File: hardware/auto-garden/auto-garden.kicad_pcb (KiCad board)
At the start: 2 copper layers, 71.1 x 55.9 mm, 30 parts, among them J1 Conn_01x02_Female, J2 Conn_01x06_Female, J3 Conn_01x03_Female, J4 Conn_01x03_Male, J5 Screw_Terminal_01x02, J6 Screw_Terminal_01x02, Q1 Q_PMOS_DGS, Q2 Q_NMOS_DGS, Q3 Q_PMOS_DGS, Q4 Q_NMOS_DGS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

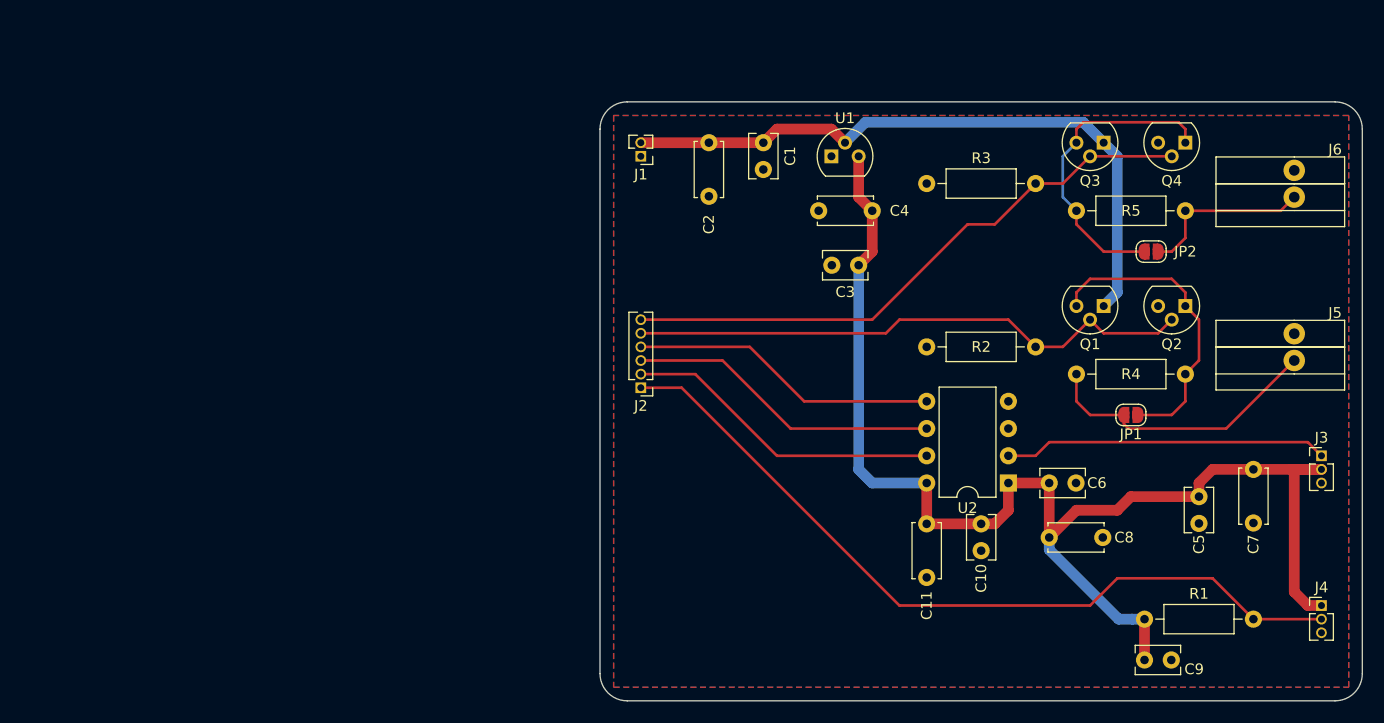
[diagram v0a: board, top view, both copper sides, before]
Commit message: Made some changes to silk screen to make assembly easier
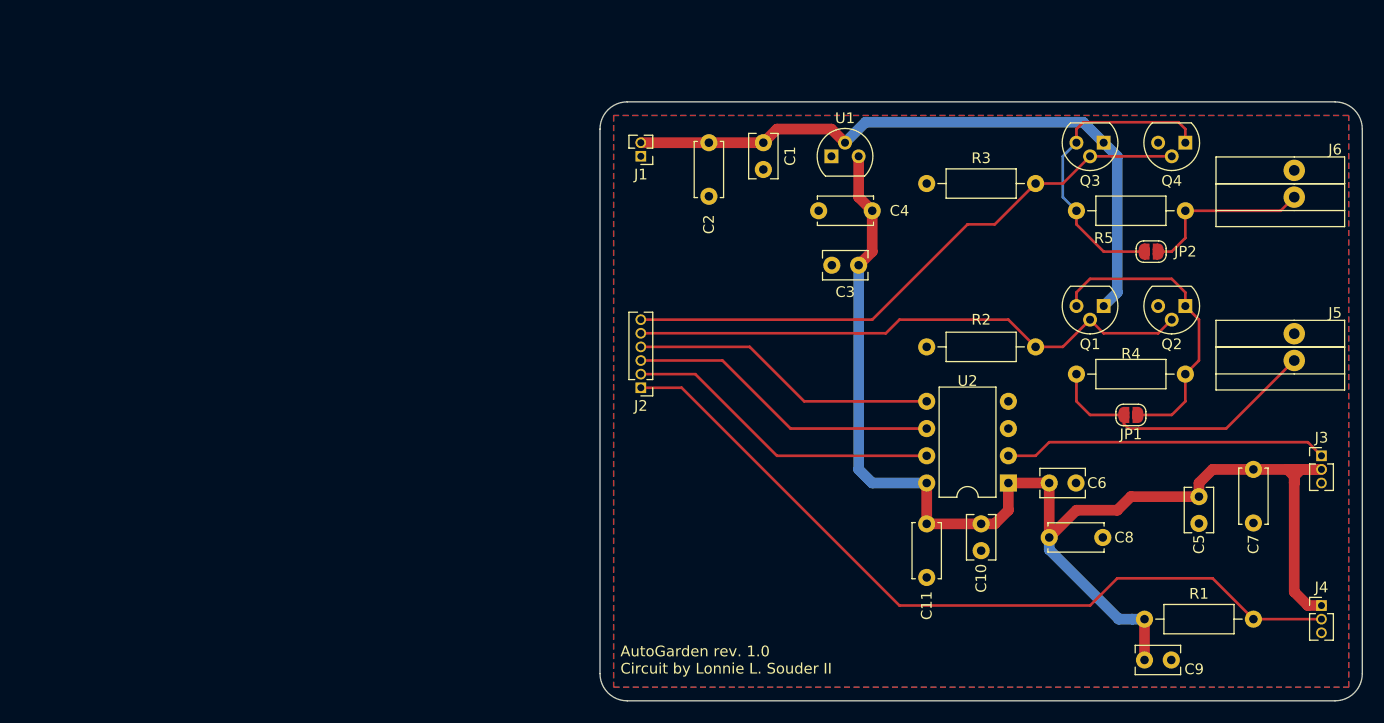
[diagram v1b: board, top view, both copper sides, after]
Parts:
- added REF**: OSHW-Logo2_7.3x6mm_SilkScreen, Symbol:OSHW-Logo2_7.3x6mm_SilkScreen, B.Cu at (125.7, 116.8)
- added REF**: KiCad-Logo2_5mm_SilkScreen, Symbol:KiCad-Logo2_5mm_SilkScreen, B.Cu at (125.7, 124.5)
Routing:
- net +3V3: track 123.6 -> 126.0 mm
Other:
- board text added: "AutoGarden rev. 1.0 Circuit by Lonnie L. Souder II"

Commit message: Added pin descriptions to silk screen
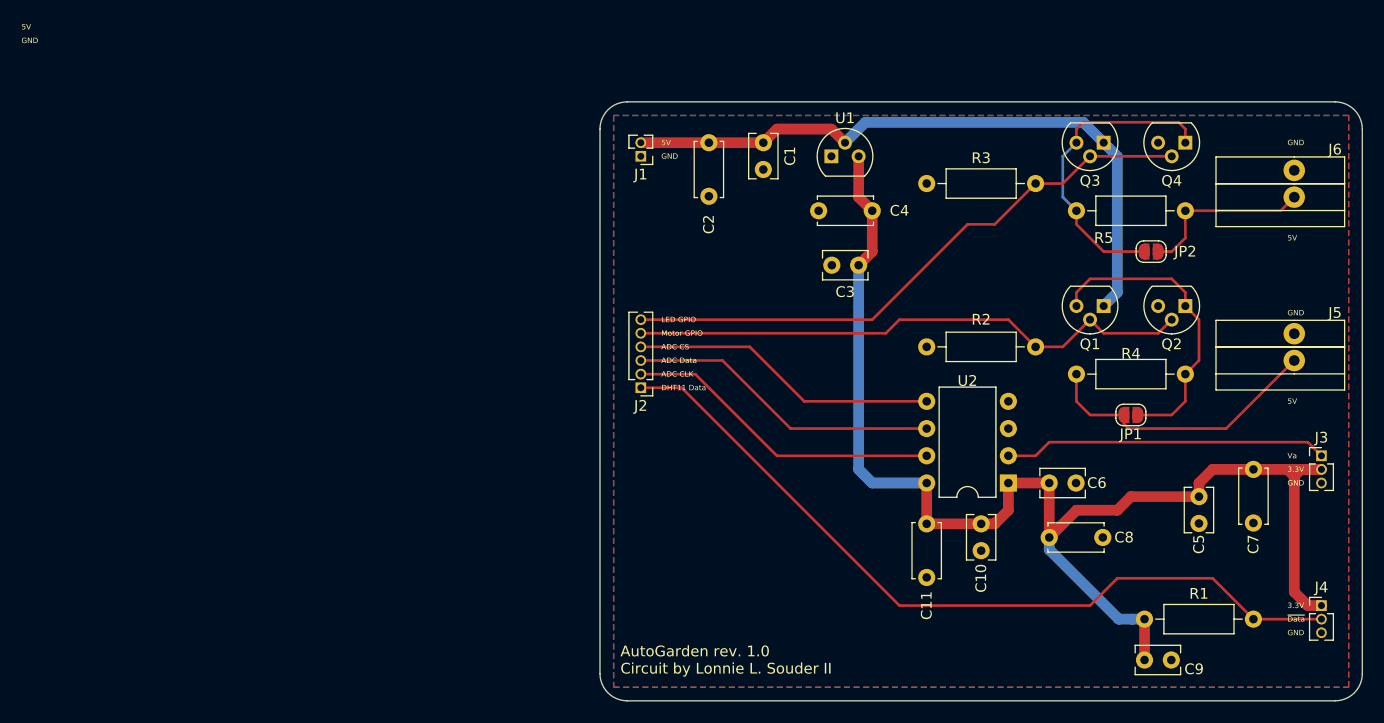
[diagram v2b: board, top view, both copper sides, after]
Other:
- board text added: "3.3V"
- board text added: "5V"
- board text added: "ADC CLK"
- board text added: "ADC CS"
- board text added: "ADC Data"
- board text added: "DHT11 Data"
- board text added: "GND"
- board text added: "LED GPIO"
- board text added: "Motor GPIO"
- board text added: "Va"
- board text added: "~Data"
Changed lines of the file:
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@@
   (general
     (thickness 1.6)
-    (drawings 9)
+    (drawings 29)
     (tracks 123)
     (zones 0)
@@
     )
   )
+  (gr_text ~Data (at 181.61 121.285) (layer F.SilkS)
+    (effects (font (size 0.5 0.5) (thickness 0.075)) (justify left))
+  )
+  (gr_text 3.3V (at 181.61 120.015) (layer F.SilkS)
+    (effects (font (size 0.5 0.5) (thickness 0.075)) (justify left))
+  )
+  (gr_text 3.3V (at 181.61 107.315) (layer F.SilkS)
+    (effects (font (size 0.5 0.5) (thickness 0.075)) (justify left))
+  )
+  (gr_text GND (at 181.61 122.555) (layer F.SilkS)
+    (effects (font (size 0.5 0.5) (thickness 0.075)) (justify left))
+  )
+  (gr_text GND (at 181.61 108.585) (layer F.SilkS)
+    (effects (font (size 0.5 0.5) (thickness 0.075)) (justify left))
+  )
+  (gr_text Va (at 181.61 106.045) (layer F.SilkS)
+    (effects (font (size 0.5 0.5) (thickness 0.075)) (justify left))
+  )
+  (gr_text GND (at 181.61 76.835) (layer F.SilkS)
+    (effects (font (size 0.5 0.5) (thickness 0.075)) (justify left))
+  )
+  (gr_text 5V (at 181.61 85.725) (layer F.SilkS)
+    (effects (font (size 0.5 0.5) (thickness 0.075)) (justify left))
+  )
+  (gr_text GND (at 181.61 92.71) (layer F.SilkS)
+    (effects (font (size 0.5 0.5) (thickness 0.075)) (justify left))
+  )
+  (gr_text 5V (at 181.61 100.965) (layer F.SilkS)
+    (effects (font (size 0.5 0.5) (thickness 0.075)) (justify left))
+  )
+  (gr_text GND (at 63.5 67.31) (layer F.SilkS)
+    (effects (font (size 0.5 0.5) (thickness 0.075)) (justify left))
+  )
+  (gr_text 5V (at 63.5 66.04) (layer F.SilkS)
+    (effects (font (size 0.5 0.5) (thickness 0.075)) (justify left))
+  )
+  (gr_text GND (at 123.19 78.105) (layer F.SilkS)
+    (effects (font (size 0.5 0.5) (thickness 0.075)) (justify left))
+  )
+  (gr_text 5V (at 123.19 76.835) (layer F.SilkS)
+    (effects (font (size 0.5 0.5) (thickness 0.075)) (justify left))
+  )
+  (gr_text "LED GPIO" (at 123.19 93.345) (layer F.SilkS)
+    (effects (font (size 0.5 0.5) (thickness 0.075)) (justify left))
+  )
+  (gr_text "Motor GPIO" (at 123.19 94.615) (layer F.SilkS)
+    (effects (font (size 0.5 0.5) (thickness 0.075)) (justify left))
+  )
+  (gr_text "ADC CS" (at 123.19 95.885) (layer F.SilkS)
+    (effects (font (size 0.5 0.5) (thickness 0.075)) (justify left))
+  )
+  (gr_text "ADC Data" (at 123.19 97.155) (layer F.SilkS)
+    (effects (font (size 0.5 0.5) (thickness 0.075)) (justify left))
+  )
+  (gr_text "ADC CLK" (at 123.19 98.425) (layer F.SilkS)
+    (effects (font (size 0.5 0.5) (thickness 0.075)) (justify left))
+  )
+  (gr_text "DHT11 Data" (at 123.19 99.695) (layer F.SilkS)
+    (effects (font (size 0.5 0.5) (thickness 0.075)) (justify left))
+  )
   (gr_text "AutoGarden rev. 1.0\nCircuit by Lonnie L. Souder II" (at 119.38 125.095) (layer F.SilkS)
